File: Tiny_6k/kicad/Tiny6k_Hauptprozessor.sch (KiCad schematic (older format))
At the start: 81 parts, among them Q100 8 MHz, X100 Port 2, X101 Port 3, X102 BUSY, X103 AC in, X104 Batterie, X105 Reset, X106 Bankumschaltung, X110 Modul 2, X120 XTAL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

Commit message: Vcc Anschluss am RAM korrigiert
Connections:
- net +5V: no longer D25.28 (VCC)
- net +5VP: now also D25.28 (VCC)
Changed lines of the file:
@@
 Sheet 2 6
 Title "JU+TE Tiny\\nHauptprozessor"
-Date "27.11.21"
-Rev "1"
+Date "13.12.21"
+Rev "2"
 Comp "Jugend+Technik"
 Comment1 ""
@@
 L power:+5V #PWR0110
 U 1 1 61984ADD
-P 5900 1450
-F 0 "#PWR0110" H 5900 1300 50  0001 C CNN
-F 1 "+5V" H 6000 1550 50  0000 C CNN
-F 2 "" H 5900 1450 50  0001 C CNN
-F 3 "" H 5900 1450 50  0001 C CNN
-	1    5900 1450
-	1    0    0    -1
+P 5150 6300
+F 0 "#PWR0110" H 5150 6150 50  0001 C CNN
+F 1 "+5V" V 5150 6500 50  0000 C CNN
+F 2 "" H 5150 6300 50  0001 C CNN
+F 3 "" H 5150 6300 50  0001 C CNN
+	1    5150 6300
+	0    -1   -1   0
 $EndComp
 $Comp
@@
 Wire Wire Line
 	5350 6500 5400 6500
-Connection ~ 5350 6500
 Wire Wire Line
-	5350 6400 5350 6500
-$Comp
-L power:+5V #PWR0116
-U 1 1 61A8516A
-P 5150 6300
-F 0 "#PWR0116" H 5150 6150 50  0001 C CNN
-F 1 "+5V" V 5150 6500 50  0000 C CNN
-F 2 "" H 5150 6300 50  0001 C CNN
-F 3 "" H 5150 6300 50  0001 C CNN
-	1    5150 6300
-	0    -1   -1   0
-$EndComp
+	5350 6400 5350 6450
 Wire Wire Line
 	5150 6300 5250 6300
@@
 	5250 6700 5250 6600
 Connection ~ 5250 6600
-Wire Wire Line
-	5200 6500 5350 6500
-Text GLabel 5200 6500 0    50   Input ~ 0
+Text GLabel 5150 6450 0    50   Input ~ 0
 ~CS0
 Text GLabel 4500 1500 2    39   Output ~ 0
@@
 Wire Wire Line
 	2650 7800 2650 7300
+$Comp
+L power:+5VP #PWR?
+U 1 1 61BBA231
+P 5900 1450
+F 0 "#PWR?" H 5900 1300 50  0001 C CNN
+F 1 "+5VP" H 5900 1600 50  0000 C CNN
+F 2 "" H 5900 1450 50  0001 C CNN
+F 3 "" H 5900 1450 50  0001 C CNN
+	1    5900 1450
+	1    0    0    -1
+$EndComp
+Wire Wire Line
+	5150 6450 5350 6450
+Connection ~ 5350 6450
+Wire Wire Line
+	5350 6450 5350 6500
 Wire Bus Line
 	3250 1600 3250 2450

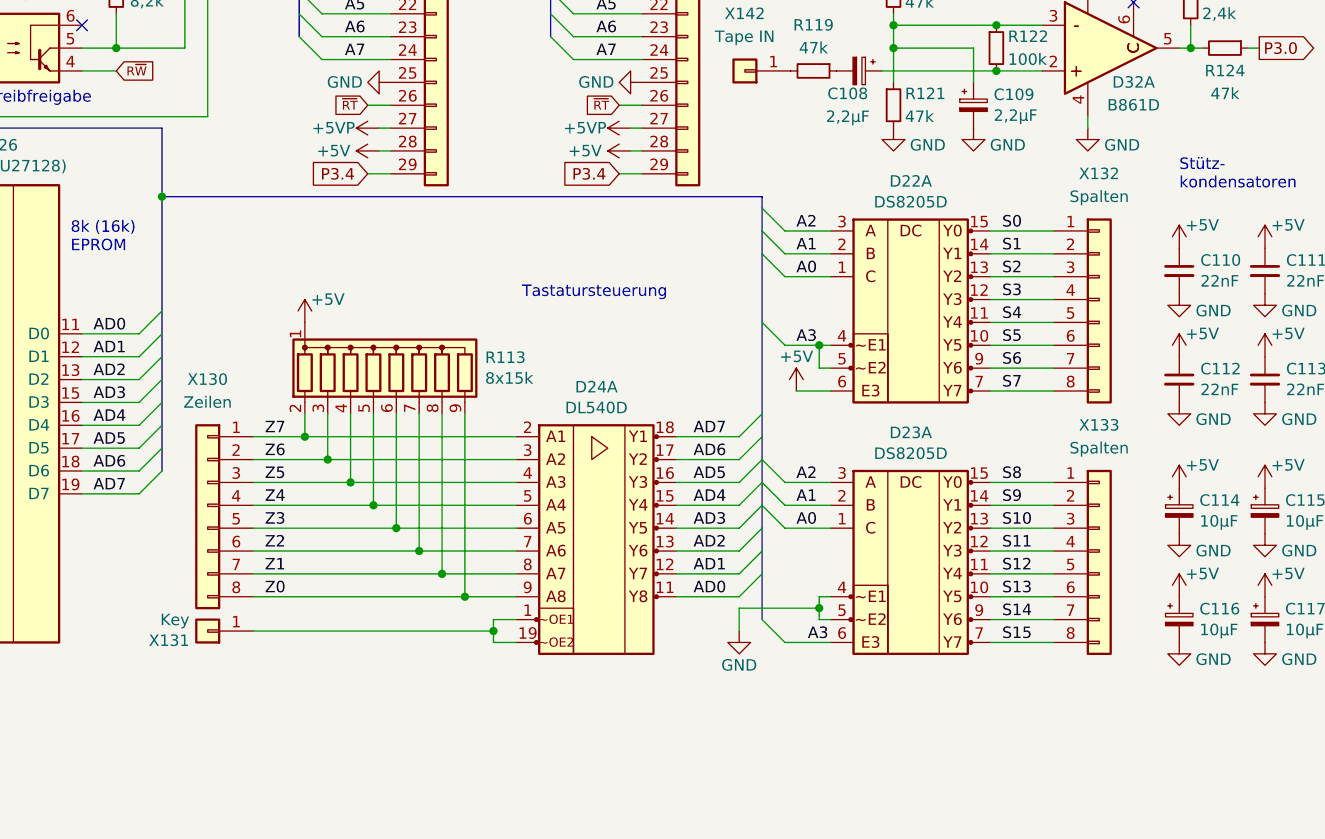
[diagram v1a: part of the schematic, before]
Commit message: change: add diodes on keyboard column lines, resolve #1
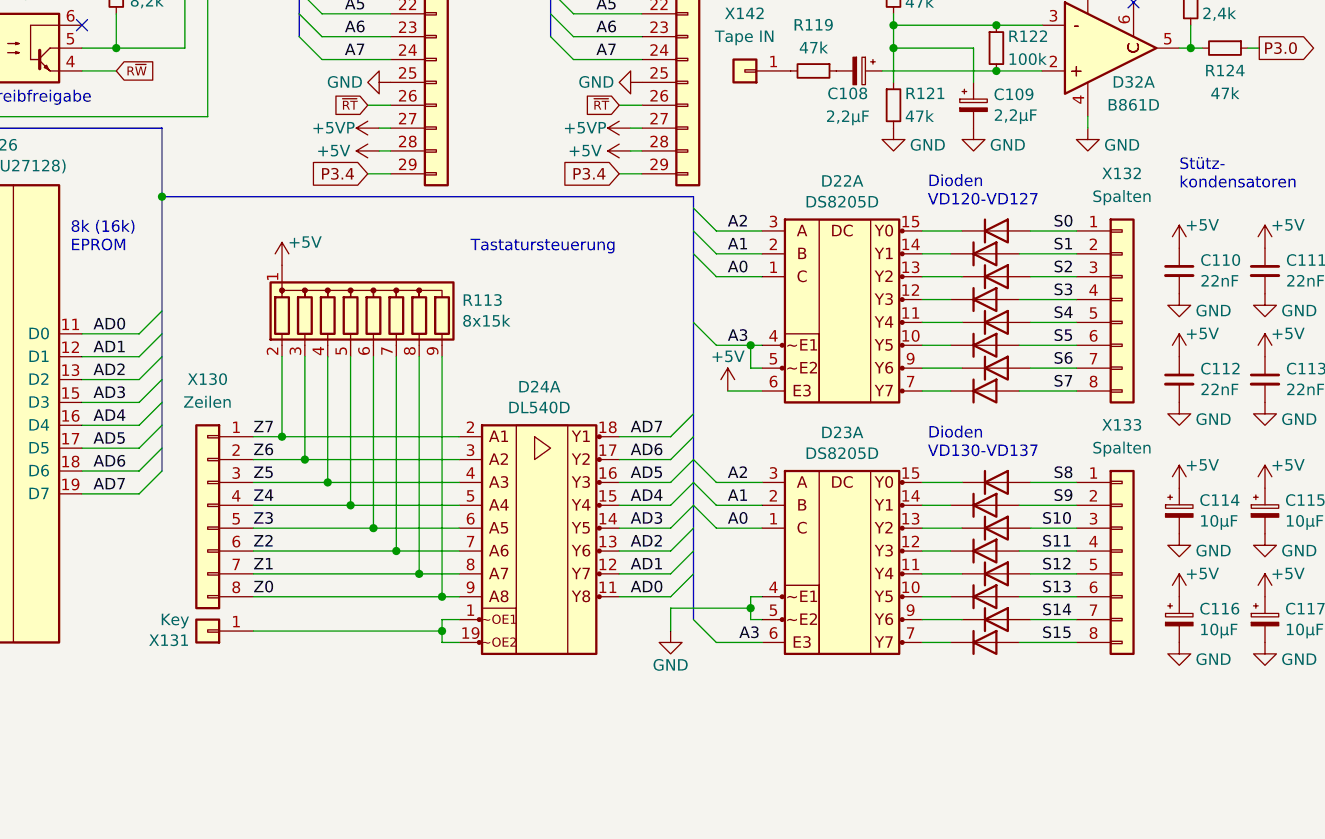
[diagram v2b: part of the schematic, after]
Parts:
- added VD120, VD121, VD122, VD123, VD124, VD125, VD126, VD127, VD130, VD131, VD132, VD133, VD134, VD135, VD136, VD137: SAY, Diode_THT:D_DO-34_SOD68_P2.54mm_Vertical_AnodeUp, symbol Device:D
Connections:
- net S0: now also VD120.2 (A); no longer D22.15 (Y0)
- net S1: now also VD121.2 (A); no longer D22.14 (Y1)
- net S10: now also VD132.2 (A); no longer D23.13 (Y2)
- net S11: now also VD133.2 (A); no longer D23.12 (Y3)
- net S12: now also VD134.2 (A); no longer D23.11 (Y4)
- net S13: now also VD135.2 (A); no longer D23.10 (Y5)
- net S14: now also VD136.2 (A); no longer D23.9 (Y6)
- net S15: now also VD137.2 (A); no longer D23.7 (Y7)
- net S2: now also VD122.2 (A); no longer D22.13 (Y2)
- net S3: now also VD123.2 (A); no longer D22.12 (Y3)
- net S4: now also VD124.2 (A); no longer D22.11 (Y4)
- net S5: now also VD125.2 (A); no longer D22.10 (Y5)
- net S6: now also VD126.2 (A); no longer D22.9 (Y6)
- net S7: now also VD127.2 (A); no longer D22.7 (Y7)
- net S8: now also VD130.2 (A); no longer D23.15 (Y0)
- net S9: now also VD131.2 (A); no longer D23.14 (Y1)
- new net: D22.10 (Y5), VD125.1 (K)
- new net: D22.11 (Y4), VD124.1 (K)
- new net: D22.12 (Y3), VD123.1 (K)
- new net: D22.13 (Y2), VD122.1 (K)
- new net: D22.14 (Y1), VD121.1 (K)
- new net: D22.15 (Y0), VD120.1 (K)
- new net: D22.7 (Y7), VD127.1 (K)
- new net: D22.9 (Y6), VD126.1 (K)
- new net: D23.10 (Y5), VD135.1 (K)
- new net: D23.11 (Y4), VD134.1 (K)
- new net: D23.12 (Y3), VD133.1 (K)
- new net: D23.13 (Y2), VD132.1 (K)
- new net: D23.14 (Y1), VD131.1 (K)
- new net: D23.15 (Y0), VD130.1 (K)
- new net: D23.7 (Y7), VD137.1 (K)
- new net: D23.9 (Y6), VD136.1 (K)
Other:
- note added: "Dioden\nVD120-VD127"
- note added: "Dioden\nVD130-VD137"
- moved on the sheet: D22A, D23A, D24A, R113, X132, X133
